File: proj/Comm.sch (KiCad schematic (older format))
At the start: 18 parts, among them J1 MicroUSB-B, U13 FT230XS

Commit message: Lots of layout work
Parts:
- U13: value FT230XS -> FT230XS_DNP
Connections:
- net IN_USBD_N is gone; now on net USBD_N: DZ10.2, R87.1, U13.9 (USB-)
- net IN_USBD_P is gone; now on net USBD_P: DZ10.4, R88.1, U13.8 (USB+)
- net USBD_N: no longer C90.1, J1.2 (D-), R87.2
- net USBD_P: no longer C91.1, J1.3 (D+), R88.2
- new net OUT_USBD_N: C90.1, J1.2 (D-), R87.2
- new net OUT_USBD_P: C91.1, J1.3 (D+), R88.2
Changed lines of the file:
@@
 P 7300 3300
 F 0 "U13" H 7300 4150 50  0000 C CNN
-F 1 "FT230XS" H 7300 4050 50  0000 C CNN
+F 1 "FT230XS_DNP" H 7300 4050 50  0000 C CNN
 F 2 "IPC7351-Nominal:SOP63P600X160-16" H 7300 3300 50  0001 C CNN
 F 3 "" H 7300 3300 60  0000 C CNN
@@
 $EndComp
 $Comp
-L GND #PWR037
+L GND #PWR044
 U 1 1 54F70105
 P 2800 3950
-F 0 "#PWR037" H 2800 3950 30  0001 C CNN
+F 0 "#PWR044" H 2800 3950 30  0001 C CNN
 F 1 "GND" H 2800 3880 30  0001 C CNN
 F 2 "" H 2800 3950 60  0000 C CNN
@@
 $EndComp
 $Comp
-L GND #PWR038
+L GND #PWR045
 U 1 1 54F7013A
 P 3250 3950
-F 0 "#PWR038" H 3250 3950 30  0001 C CNN
+F 0 "#PWR045" H 3250 3950 30  0001 C CNN
 F 1 "GND" H 3250 3880 30  0001 C CNN
 F 2 "" H 3250 3950 60  0000 C CNN
@@
 $EndComp
 $Comp
-L GND #PWR039
+L GND #PWR046
 U 1 1 54F70169
 P 4350 4000
-F 0 "#PWR039" H 4350 4000 30  0001 C CNN
+F 0 "#PWR046" H 4350 4000 30  0001 C CNN
 F 1 "GND" H 4350 3930 30  0001 C CNN
 F 2 "" H 4350 4000 60  0000 C CNN
@@
 $EndComp
 $Comp
-L GND #PWR040
+L GND #PWR047
 U 1 1 54F7019B
 P 2100 3500
-F 0 "#PWR040" H 2100 3500 30  0001 C CNN
+F 0 "#PWR047" H 2100 3500 30  0001 C CNN
 F 1 "GND" H 2100 3430 30  0001 C CNN
 F 2 "" H 2100 3500 60  0000 C CNN
@@
 $EndComp
 $Comp
-L GND #PWR041
+L GND #PWR048
 U 1 1 54F716C5
 P 1800 4300
-F 0 "#PWR041" H 1800 4300 30  0001 C CNN
+F 0 "#PWR048" H 1800 4300 30  0001 C CNN
 F 1 "GND" H 1800 4230 30  0001 C CNN
 F 2 "" H 1800 4300 60  0000 C CNN
@@
 $EndComp
 $Comp
-L GND #PWR042
+L GND #PWR049
 U 1 1 54F71702
 P 1600 4300
-F 0 "#PWR042" H 1600 4300 30  0001 C CNN
+F 0 "#PWR049" H 1600 4300 30  0001 C CNN
 F 1 "GND" H 1600 4230 30  0001 C CNN
 F 2 "" H 1600 4300 60  0000 C CNN
@@
 USBSHIELD
 Text Label 2850 3100 0    50   ~ 0
-USBD_N
+OUT_USBD_N
 Text Label 2850 3200 0    50   ~ 0
-USBD_P
+OUT_USBD_P
 Text Label 5250 3100 0    50   ~ 0
 IN_USBD_N
@@
 $EndComp
 $Comp
-L GND #PWR043
+L GND #PWR050
 U 1 1 54F71E1B
 P 2300 4300
-F 0 "#PWR043" H 2300 4300 30  0001 C CNN
+F 0 "#PWR050" H 2300 4300 30  0001 C CNN
 F 1 "GND" H 2300 4230 30  0001 C CNN
 F 2 "" H 2300 4300 60  0000 C CNN
@@
 $EndComp
 $Comp
-L GND #PWR044
+L GND #PWR051
 U 1 1 54F7543C
 P 5000 2900
-F 0 "#PWR044" H 5000 2900 30  0001 C CNN
+F 0 "#PWR051" H 5000 2900 30  0001 C CNN
 F 1 "GND" H 5000 2830 30  0001 C CNN
 F 2 "" H 5000 2900 60  0000 C CNN
@@
 $EndComp
 $Comp
-L GND #PWR045
+L GND #PWR052
 U 1 1 54F75AA1
 P 5450 2650
-F 0 "#PWR045" H 5450 2650 30  0001 C CNN
+F 0 "#PWR052" H 5450 2650 30  0001 C CNN
 F 1 "GND" H 5450 2580 30  0001 C CNN
 F 2 "" H 5450 2650 60  0000 C CNN
@@
 $EndComp
 $Comp
-L GND #PWR046
+L GND #PWR053
 U 1 1 54F76B86
 P 6100 2900
-F 0 "#PWR046" H 6100 2900 30  0001 C CNN
+F 0 "#PWR053" H 6100 2900 30  0001 C CNN
 F 1 "GND" H 6100 2830 30  0001 C CNN
 F 2 "" H 6100 2900 60  0000 C CNN
@@
 $EndComp
 $Comp
-L GND #PWR047
+L GND #PWR054
 U 1 1 54F76CB4
 P 6600 4000
-F 0 "#PWR047" H 6600 4000 30  0001 C CNN
+F 0 "#PWR054" H 6600 4000 30  0001 C CNN
 F 1 "GND" H 6600 3930 30  0001 C CNN
 F 2 "" H 6600 4000 60  0000 C CNN
@@
 $EndComp
 $Comp
-L GND #PWR048
+L GND #PWR055
 U 1 1 54F76DBE
 P 8000 4000
-F 0 "#PWR048" H 8000 4000 30  0001 C CNN
+F 0 "#PWR055" H 8000 4000 30  0001 C CNN
 F 1 "GND" H 8000 3930 30  0001 C CNN
 F 2 "" H 8000 4000 60  0000 C CNN
@@
 $EndComp
 $Comp
-L GND #PWR049
+L GND #PWR056
 U 1 1 54F81F0B
 P 8200 2650
-F 0 "#PWR049" H 8200 2650 30  0001 C CNN
+F 0 "#PWR056" H 8200 2650 30  0001 C CNN
 F 1 "GND" H 8200 2580 30  0001 C CNN
 F 2 "" H 8200 2650 60  0000 C CNN
@@
 	4350 3500 4350 2300
 Connection ~ 4350 2300
+Text HLabel 5900 3300 2    50   BiDi ~ 0
+USBD_N
+Wire Wire Line
+	5900 3300 5800 3300
+Wire Wire Line
+	5800 3300 5800 3100
+Connection ~ 5800 3100
+Text HLabel 5900 3400 2    50   BiDi ~ 0
+USBD_P
+Wire Wire Line
+	5900 3400 5700 3400
+Wire Wire Line
+	5700 3400 5700 3200
+Connection ~ 5700 3200
 $EndSCHEMATC

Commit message: Some work removing unnecessary bits
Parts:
- removed C90, C91: 47p, IPC7351-Nominal:CAPC1005X55, symbol C-0402
- removed R89: 2R2, IPC7351-Nominal:RESC1005X40, symbol R-0402
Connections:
- net GND: now also C92.2
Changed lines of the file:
@@
 $Descr A4 11693 8268
 encoding utf-8
-Sheet 3 13
+Sheet 2 13
 Title ""
 Date "2015-02-28"
@@
 $EndComp
 $Comp
-L C-0402 C90
-U 1 1 54F6FF0D
-P 2800 3700
-F 0 "C90" H 3000 3750 50  0000 C CNN
-F 1 "47p" H 3000 3650 50  0000 C CNN
-F 2 "IPC7351-Nominal:CAPC1005X55" H 2800 3700 50  0001 C CNN
-F 3 "" H 2790 3675 60  0000 C CNN
-F 4 "Value" H 2800 3700 60  0001 C CNN "Manuf"
-F 5 "CAP MLCC47p C0G 50V 10% [0402]" H 3600 4250 60  0001 C CNN "BOM"
-	1    2800 3700
-	1    0    0    -1
-$EndComp
-$Comp
-L C-0402 C91
-U 1 1 54F6FFDF
-P 3250 3700
-F 0 "C91" H 3450 3750 50  0000 C CNN
-F 1 "47p" H 3450 3650 50  0000 C CNN
-F 2 "IPC7351-Nominal:CAPC1005X55" H 3250 3700 50  0001 C CNN
-F 3 "" H 3240 3675 60  0000 C CNN
-F 4 "Value" H 3250 3700 60  0001 C CNN "Manuf"
-F 5 "CAP MLCC47p C0G 50V 10% [0402]" H 4050 4250 60  0001 C CNN "BOM"
-	1    3250 3700
-	1    0    0    -1
-$EndComp
-$Comp
 L SP0503BAHT DZ10
 U 1 1 54F70045
@@
 $Comp
 L GND #PWR026
-U 1 1 54F70105
-P 2800 3950
-F 0 "#PWR026" H 2800 3950 30  0001 C CNN
-F 1 "GND" H 2800 3880 30  0001 C CNN
-F 2 "" H 2800 3950 60  0000 C CNN
-F 3 "" H 2800 3950 60  0000 C CNN
-	1    2800 3950
-	1    0    0    -1
-$EndComp
-$Comp
-L GND #PWR027
-U 1 1 54F7013A
-P 3250 3950
-F 0 "#PWR027" H 3250 3950 30  0001 C CNN
-F 1 "GND" H 3250 3880 30  0001 C CNN
-F 2 "" H 3250 3950 60  0000 C CNN
-F 3 "" H 3250 3950 60  0000 C CNN
-	1    3250 3950
-	1    0    0    -1
-$EndComp
-$Comp
-L GND #PWR028
 U 1 1 54F70169
 P 4350 4000
-F 0 "#PWR028" H 4350 4000 30  0001 C CNN
+F 0 "#PWR026" H 4350 4000 30  0001 C CNN
 F 1 "GND" H 4350 3930 30  0001 C CNN
 F 2 "" H 4350 4000 60  0000 C CNN
@@
 $EndComp
 $Comp
-L GND #PWR029
+L GND #PWR027
 U 1 1 54F7019B
 P 2100 3500
-F 0 "#PWR029" H 2100 3500 30  0001 C CNN
+F 0 "#PWR027" H 2100 3500 30  0001 C CNN
 F 1 "GND" H 2100 3430 30  0001 C CNN
 F 2 "" H 2100 3500 60  0000 C CNN
@@
 $EndComp
 $Comp
-L GND #PWR030
+L GND #PWR028
 U 1 1 54F716C5
 P 1800 4300
-F 0 "#PWR030" H 1800 4300 30  0001 C CNN
+F 0 "#PWR028" H 1800 4300 30  0001 C CNN
 F 1 "GND" H 1800 4230 30  0001 C CNN
 F 2 "" H 1800 4300 60  0000 C CNN
@@
 $EndComp
 $Comp
-L GND #PWR031
+L GND #PWR029
 U 1 1 54F71702
 P 1600 4300
-F 0 "#PWR031" H 1600 4300 30  0001 C CNN
+F 0 "#PWR029" H 1600 4300 30  0001 C CNN
 F 1 "GND" H 1600 4230 30  0001 C CNN
 F 2 "" H 1600 4300 60  0000 C CNN
@@
 $EndComp
 $Comp
-L GND #PWR032
+L GND #PWR030
 U 1 1 54F71E1B
 P 2300 4300
-F 0 "#PWR032" H 2300 4300 30  0001 C CNN
+F 0 "#PWR030" H 2300 4300 30  0001 C CNN
 F 1 "GND" H 2300 4230 30  0001 C CNN
 F 2 "" H 2300 4300 60  0000 C CNN
@@
 $EndComp
 $Comp
-L R-0402 R89
-U 1 1 54F753E6
-P 5000 2750
-F 0 "R89" H 5200 2800 50  0000 C CNN
-F 1 "2R2" H 5200 2700 50  0000 C CNN
-F 2 "IPC7351-Nominal:RESC1005X40" H 5000 2750 50  0001 C CNN
-F 3 "" H 5000 2800 60  0000 C CNN
-F 4 "Value" H 5000 2750 60  0001 C CNN "Manuf"
-F 5 "RES SMD 2.2 5% [0402]" H 5750 3300 60  0001 C CNN "BOM"
-	1    5000 2750
-	1    0    0    -1
-$EndComp
-$Comp
-L GND #PWR033
+L GND #PWR031
 U 1 1 54F7543C
-P 5000 2900
-F 0 "#PWR033" H 5000 2900 30  0001 C CNN
-F 1 "GND" H 5000 2830 30  0001 C CNN
-F 2 "" H 5000 2900 60  0000 C CNN
-F 3 "" H 5000 2900 60  0000 C CNN
-	1    5000 2900
+P 5000 2650
+F 0 "#PWR031" H 5000 2650 30  0001 C CNN
+F 1 "GND" H 5000 2580 30  0001 C CNN
+F 2 "" H 5000 2650 60  0000 C CNN
+F 3 "" H 5000 2650 60  0000 C CNN
+	1    5000 2650
 	1    0    0    -1
 $EndComp
@@
 $EndComp
 $Comp
-L GND #PWR034
+L GND #PWR032
 U 1 1 54F75AA1
 P 5450 2650
-F 0 "#PWR034" H 5450 2650 30  0001 C CNN
+F 0 "#PWR032" H 5450 2650 30  0001 C CNN
 F 1 "GND" H 5450 2580 30  0001 C CNN
 F 2 "" H 5450 2650 60  0000 C CNN
@@
 $EndComp
 $Comp
-L GND #PWR035
+L GND #PWR033
 U 1 1 54F76B86
 P 6100 2900
-F 0 "#PWR035" H 6100 2900 30  0001 C CNN
+F 0 "#PWR033" H 6100 2900 30  0001 C CNN
 F 1 "GND" H 6100 2830 30  0001 C CNN
 F 2 "" H 6100 2900 60  0000 C CNN
@@
 $EndComp
 $Comp
-L GND #PWR036
+L GND #PWR034
 U 1 1 54F76CB4
 P 6600 4000
-F 0 "#PWR036" H 6600 4000 30  0001 C CNN
+F 0 "#PWR034" H 6600 4000 30  0001 C CNN
 F 1 "GND" H 6600 3930 30  0001 C CNN
 F 2 "" H 6600 4000 60  0000 C CNN
@@
 $EndComp
 $Comp
-L GND #PWR037
+L GND #PWR035
 U 1 1 54F76DBE
 P 8000 4000
-F 0 "#PWR037" H 8000 4000 30  0001 C CNN
+F 0 "#PWR035" H 8000 4000 30  0001 C CNN
 F 1 "GND" H 8000 3930 30  0001 C CNN
 F 2 "" H 8000 4000 60  0000 C CNN
@@
 $EndComp
 $Comp
-L GND #PWR038
+L GND #PWR036
 U 1 1 54F81F0B
 P 8200 2650
-F 0 "#PWR038" H 8200 2650 30  0001 C CNN
+F 0 "#PWR036" H 8200 2650 30  0001 C CNN
 F 1 "GND" H 8200 2580 30  0001 C CNN
 F 2 "" H 8200 2650 60  0000 C CNN
@@
 	3950 3200 6700 3200
 Wire Wire Line
-	2800 3600 2800 3100
-Connection ~ 2800 3100
-Wire Wire Line
-	3250 3200 3250 3600
-Connection ~ 3250 3200
-Wire Wire Line
-	2800 3950 2800 3800
-Wire Wire Line
-	3250 3950 3250 3800
-Wire Wire Line
 	4350 4000 4350 3950
 Wire Wire Line
@@
 	5000 2600 5000 2650
 Wire Wire Line
-	5000 2900 5000 2850
-Wire Wire Line
 	5450 2400 5450 2300

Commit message: Clean up resistor BOM
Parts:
- added R16: 3R3, IPC7351-Nominal:RESC1005X40, symbol R-0402
- R87, R88: value 27 -> 22; BOM RES SMD 27 5% [0402] -> RES SMD 22 5% [0402]
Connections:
- net GND: now also R16.2; no longer C92.2
- new net: C92.2, R16.1
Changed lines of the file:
@@
 P 3850 3200
 F 0 "R88" V 3950 3200 50  0000 C CNN
-F 1 "27" V 4050 3200 50  0000 C CNN
+F 1 "22" V 4050 3200 50  0000 C CNN
 F 2 "IPC7351-Nominal:RESC1005X40" H 3850 3200 50  0001 C CNN
 F 3 "" H 3850 3250 60  0000 C CNN
 F 4 "Value" H 3850 3200 60  0001 C CNN "Manuf"
-F 5 "RES SMD 27 5% [0402]" H 4600 3750 60  0001 C CNN "BOM"
+F 5 "RES SMD 22 5% [0402]" H 4600 3750 60  0001 C CNN "BOM"
 	1    3850 3200
 	0    1    1    0
@@
 P 3850 3100
 F 0 "R87" V 4050 3100 50  0000 C CNN
-F 1 "27" V 3950 3100 50  0000 C CNN
+F 1 "22" V 3950 3100 50  0000 C CNN
 F 2 "IPC7351-Nominal:RESC1005X40" H 3850 3100 50  0001 C CNN
 F 3 "" H 3850 3150 60  0000 C CNN
 F 4 "Value" H 3850 3100 60  0001 C CNN "Manuf"
-F 5 "RES SMD 27 5% [0402]" H 4600 3650 60  0001 C CNN "BOM"
+F 5 "RES SMD 22 5% [0402]" H 4600 3650 60  0001 C CNN "BOM"
 	1    3850 3100
 	0    1    -1   0
@@
 L GND #PWR031
 U 1 1 54F7543C
-P 5000 2650
-F 0 "#PWR031" H 5000 2650 30  0001 C CNN
-F 1 "GND" H 5000 2580 30  0001 C CNN
-F 2 "" H 5000 2650 60  0000 C CNN
-F 3 "" H 5000 2650 60  0000 C CNN
-	1    5000 2650
+P 5000 2900
+F 0 "#PWR031" H 5000 2900 30  0001 C CNN
+F 1 "GND" H 5000 2830 30  0001 C CNN
+F 2 "" H 5000 2900 60  0000 C CNN
+F 3 "" H 5000 2900 60  0000 C CNN
+	1    5000 2900
 	1    0    0    -1
 $EndComp
@@
 Connection ~ 5000 2300
 Wire Wire Line
-	5000 2600 5000 2650
-Wire Wire Line
 	5450 2400 5450 2300
 Connection ~ 5450 2300
@@
 	5700 3400 5700 3200
 Connection ~ 5700 3200
+$Comp
+L R-0402 R16
+U 1 1 54FD1BAB
+P 5000 2750
+F 0 "R16" H 5200 2800 50  0000 C CNN
+F 1 "3R3" H 5200 2700 50  0000 C CNN
+F 2 "IPC7351-Nominal:RESC1005X40" H 5000 2750 50  0001 C CNN
+F 3 "" H 5000 2800 60  0000 C CNN
+F 4 "Value" H 5000 2750 60  0001 C CNN "Manuf"
+F 5 "RES SMD 3.3 5% [0402]" H 5750 3300 60  0001 C CNN "BOM"
+	1    5000 2750
+	1    0    0    -1
+$EndComp
+Wire Wire Line
+	5000 2650 5000 2600
+Wire Wire Line
+	5000 2850 5000 2900
 $EndSCHEMATC

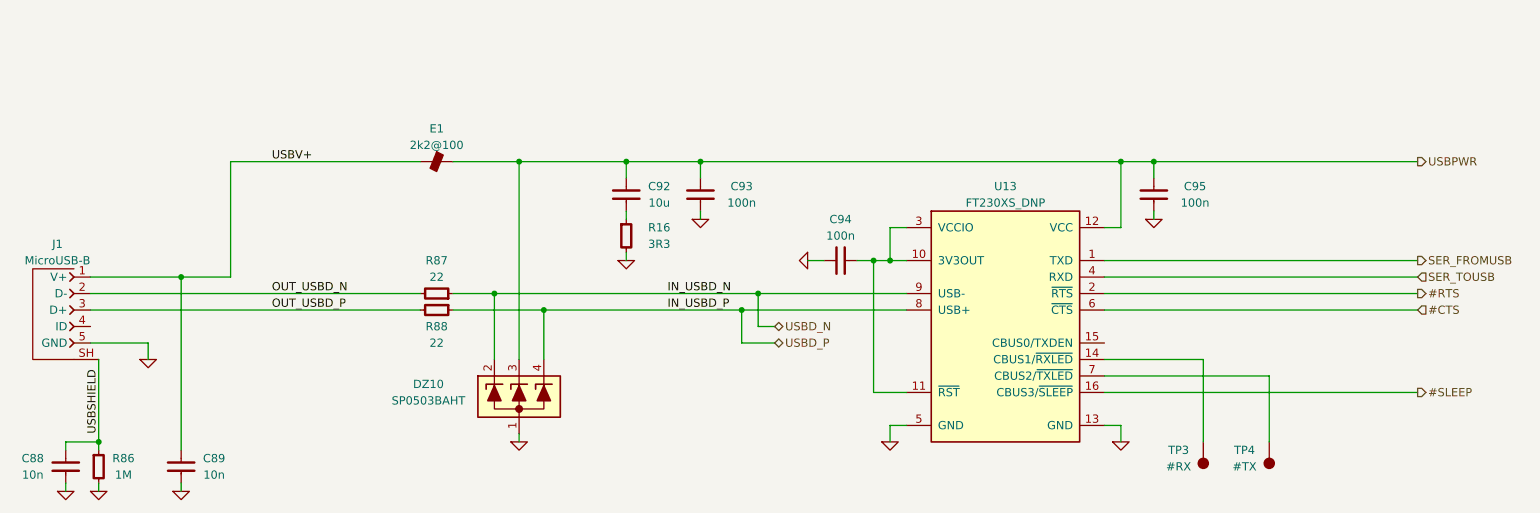
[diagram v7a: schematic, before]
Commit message: Swap 0402 to 0603, add USB inrush protection
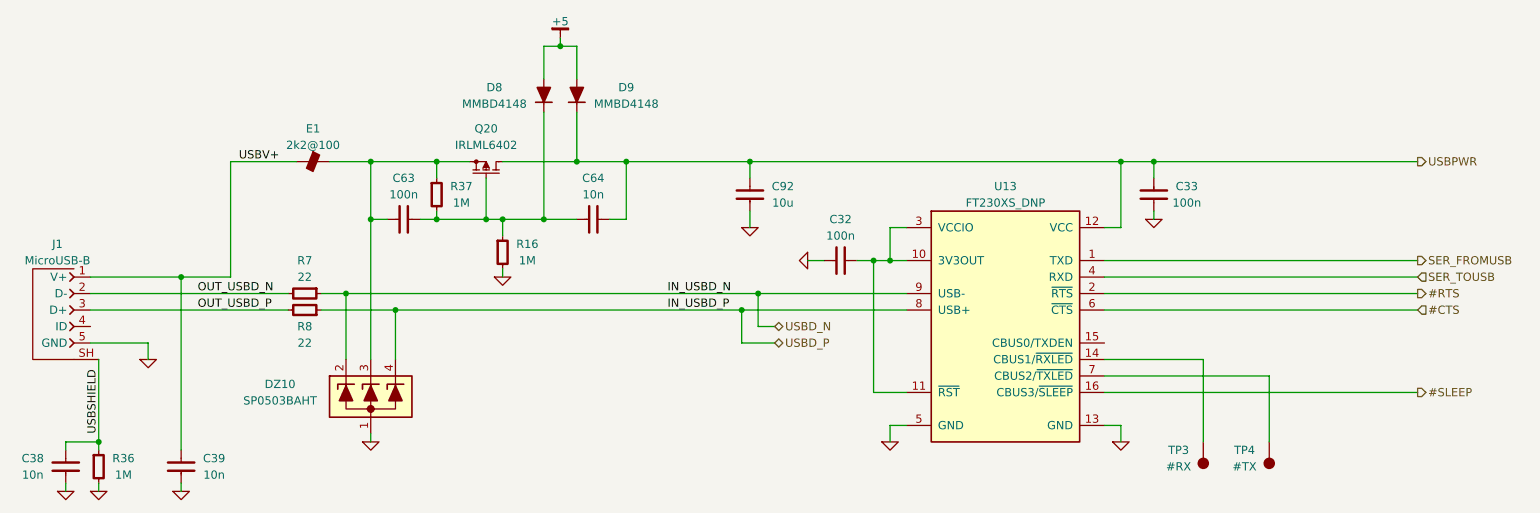
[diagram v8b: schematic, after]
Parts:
- removed C88, C89: 10n, IPC7351-Nominal:CAPC1005X55, symbol C-0402
- removed C93, C94, C95: 100n, IPC7351-Nominal:CAPC2012X70, symbol C-0805
- removed R16: 3R3, IPC7351-Nominal:RESC1005X40, symbol R-0402
- removed R86: 1M, IPC7351-Nominal:RESC1005X40, symbol R-0402
- removed R87, R88: 22, IPC7351-Nominal:RESC1005X40, symbol R-0402
- added C32, C33, C63: 100n, IPC7351-Nominal:CAPC1608X55, symbol C-0603
- added C38, C39, C64: 10n, IPC7351-Nominal:CAPC1608X55, symbol C-0603
- added D8, D9: MMBD4148, smd-semi:SOT-23, symbol MMBD4148
- added Q20: IRLML6402, smd-semi:SOT-23, symbol IRLML6402
- added R16, R36, R37: 1M, IPC7351-Nominal:RESC1608X50, symbol R-0603
- added R7, R8: 22, IPC7351-Nominal:RESC1608X50, symbol R-0603
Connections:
- net GND: now also C92.2, C32.2, C33.1, C38.2, C39.2, R16.2, R36.2
- net OUT_USBD_N: now also R7.2
- net OUT_USBD_P: now also R8.2
- net USBD_N: now also R7.1
- net USBD_P: now also R8.1
- net USBPWR: now also C33.2, C64.1, D9.3, Q20.3; no longer DZ10.3, E1.2
- net USBSHIELD: now also C38.1, R36.1
- net USBV+: now also C39.1
- net at U13.10 (3V3OUT), U13.11 (~RST), U13.3 (VCCIO): now also C32.1
- new net: C63.2, DZ10.3, E1.2, Q20.2, R37.1
- new net: C63.1, C64.2, D8.3, Q20.1, R16.1, R37.2
- new net +5: D8.1, D9.1
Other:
- moved on the sheet: C92, DZ10, E1
